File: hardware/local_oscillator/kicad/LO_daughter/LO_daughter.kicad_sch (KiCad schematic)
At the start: 39 parts, among them J1 Conn_01x09, J2 Conn_01x09, U1 ADF5355, U2 NCR2-113+, U3 SMA-J-P-H-ST-TH1

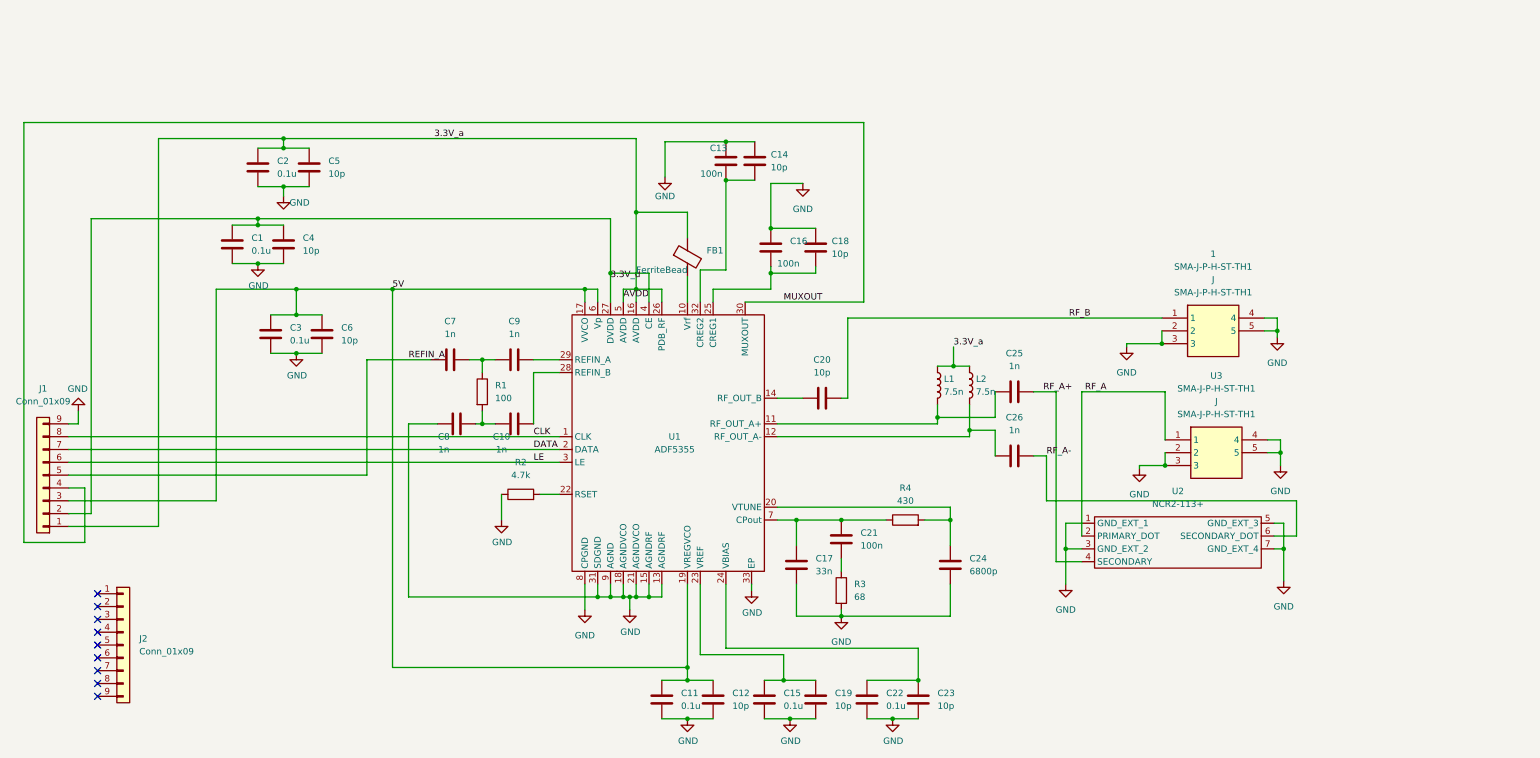
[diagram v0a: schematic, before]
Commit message: Update APC and LO
1) Add 30dB of fixed attenuation in feedback line of APC for better
   linearity of the power meter
2) Add power splitter for single ended outputs of the local oscillator
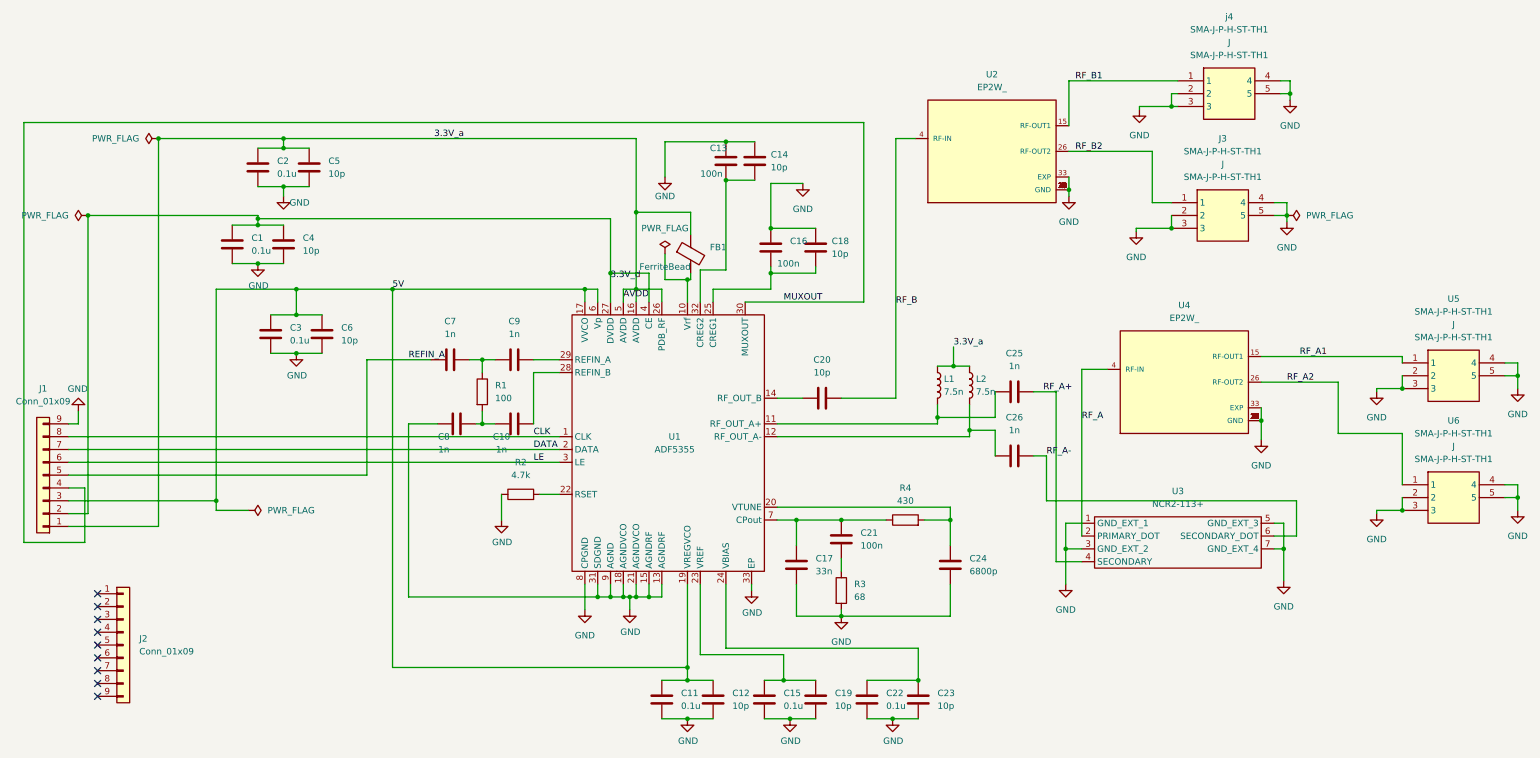
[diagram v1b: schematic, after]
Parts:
- added J3, U6: SMA-J-P-H-ST-TH1, footprints:SMAJPHSTTH1, symbol Connettori_sma_nuovi:SMA-J-P-H-ST-TH1
- added U2, U4: EP2W_, footprints:QFN51P500X500X99-33N, symbol EP2W_:EP2W_
- U5: renamed from U3; footprint Connettori_sma_verticali:SMAJPHSTTH1 -> footprints:SMAJPHSTTH1
- j4: renamed from 1; footprint Connettori_sma_verticali:SMAJPHSTTH1 -> footprints:SMAJPHSTTH1
- renumbered U2 to U3
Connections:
- net GND: now also J3.2, J3.3, J3.4, J3.5, U2.1 (GND), U2.10 (GND), U2.11 (GND), U2.12 (GND), U2.13 (GND), U2.14 (GND), U2.16 (GND), U2.17 (GND), U2.18 (GND), U2.19 (GND), U2.2 (GND), U2.20 (GND), U2.21 (GND), U2.22 (GND), U2.23 (GND), U2.24 (GND), U2.25 (GND), U2.27 (GND), U2.28 (GND), U2.29 (GND), U2.3 (GND), U2.30 (GND), U2.31 (GND), U2.32 (GND), U2.33 (EXP), U2.5 (GND), U2.6 (GND), U2.7 (GND), U2.8 (GND), U2.9 (GND), U4.1 (GND), U4.10 (GND), U4.11 (GND), U4.12 (GND), U4.13 (GND), U4.14 (GND), U4.16 (GND), U4.17 (GND), U4.18 (GND), U4.19 (GND), U4.2 (GND), U4.20 (GND), U4.21 (GND), U4.22 (GND), U4.23 (GND), U4.24 (GND), U4.25 (GND), U4.27 (GND), U4.28 (GND), U4.29 (GND), U4.3 (GND), U4.30 (GND), U4.31 (GND), U4.32 (GND), U4.33 (EXP), U4.5 (GND), U4.6 (GND), U4.7 (GND), U4.8 (GND), U4.9 (GND), U6.2, U6.3, U6.4, U6.5
- net RF_A: now also U4.4 (RF-IN); no longer U5.1
- net RF_B: now also U2.4 (RF-IN); no longer j4.1
- new net RF_A1: U4.15 (RF-OUT1), U5.1
- new net RF_A2: U4.26 (RF-OUT2), U6.1
- new net RF_B1: U2.15 (RF-OUT1), j4.1
- new net RF_B2: J3.1, U2.26 (RF-OUT2)
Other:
- moved on the sheet: FB1, U5, j4

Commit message: Update BOMs
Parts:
- C1, C11, C13, C15, C16, C17, C2, C22, C3, R2: Package (none) -> 0805
- C10, C7, C8, C9, L1, L2, R4: Package (none) -> 0402
- C12, C14, C18, C19, C20, C23, C4, C5, C6, R1, R3: Package (none) -> 0603
- C21: Package (none) -> 1206
- C24: Package (none) -> 0201
- FB1: LCSC Part # (none) -> C668299; Manufacturer_Part_Number (none) -> BLM15AX100SN1D; Mouser Part Number (none) -> 81-BLM15AX100SN1D; Mouser Price/Stock (none) -> https://www.mouser.it/ProductDetail/Murata-Electronics/BLM1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
- U1: Manufacturer_Part_Number (none) -> ADF5355BCPZ; Mouser Part Number (none) -> 584-ADF5355BCPZ; Mouser Price/Stock (none) -> https://www.mouser.it/ProductDetail/Analog-Devices/ADF5355B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
- U2, U4: LCSC Part # (none) -> C3154895; Manufacturer_Part_Number (none) -> EP2W+; Mouser Part Number (none) -> 139-EP2W; Mouser Price/Stock (none) -> https://www.mouser.it/ProductDetail/Mini-Circuits/EP2W%2b?q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
- U3: LCSC Part # (none) -> C3304869; Manufacturer_Part_Number (none) -> NCR2-113+; Mouser Part Number (none) -> 139-NCR2-113; Mouser Price/Stock (none) -> https://www.mouser.it/ProductDetail/Mini-Circuits/NCR2-113%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
